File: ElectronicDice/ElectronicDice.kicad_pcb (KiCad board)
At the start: 2 copper layers, 17 parts, among them J1 Conn_01x02_Pin, SW1 SW_Push

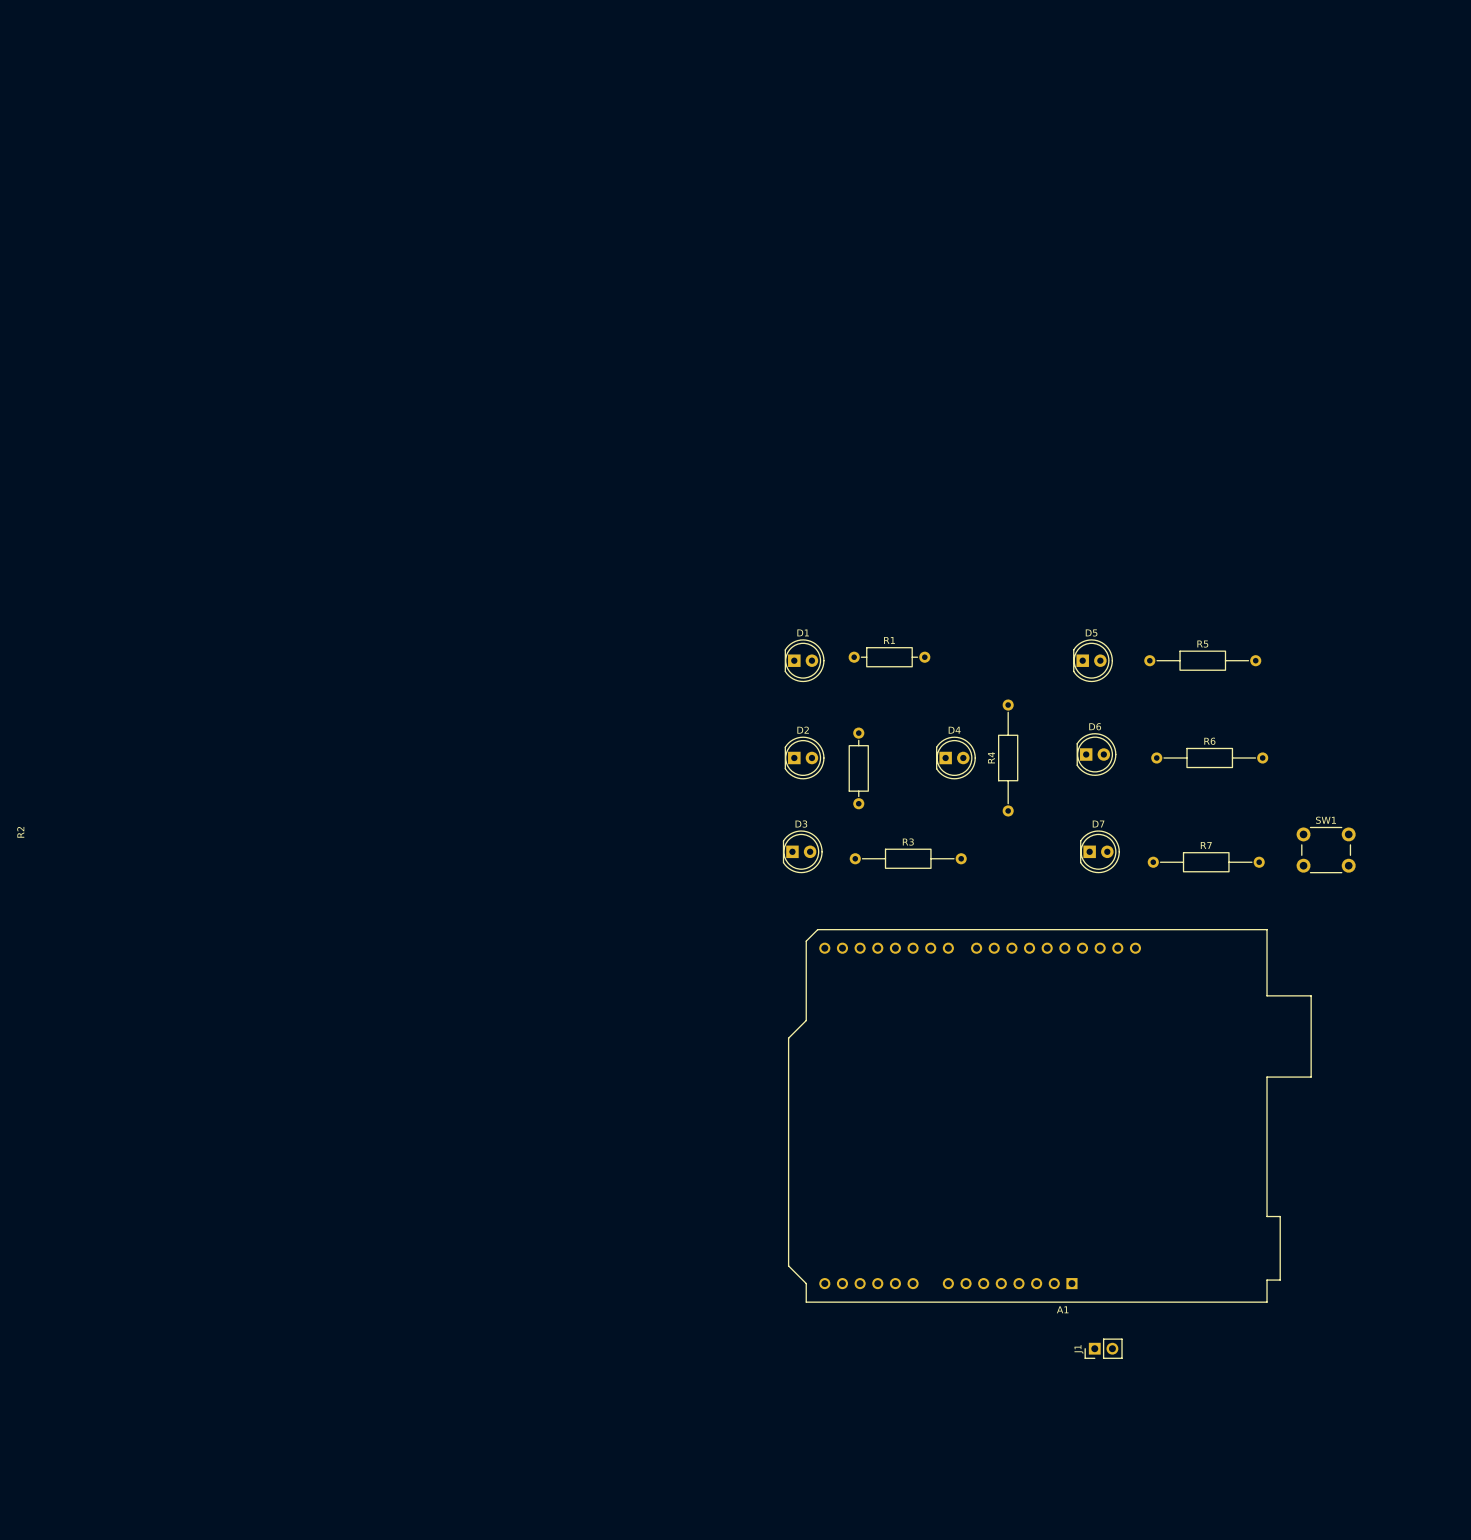
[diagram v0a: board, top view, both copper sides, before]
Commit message: Added connections in PCB
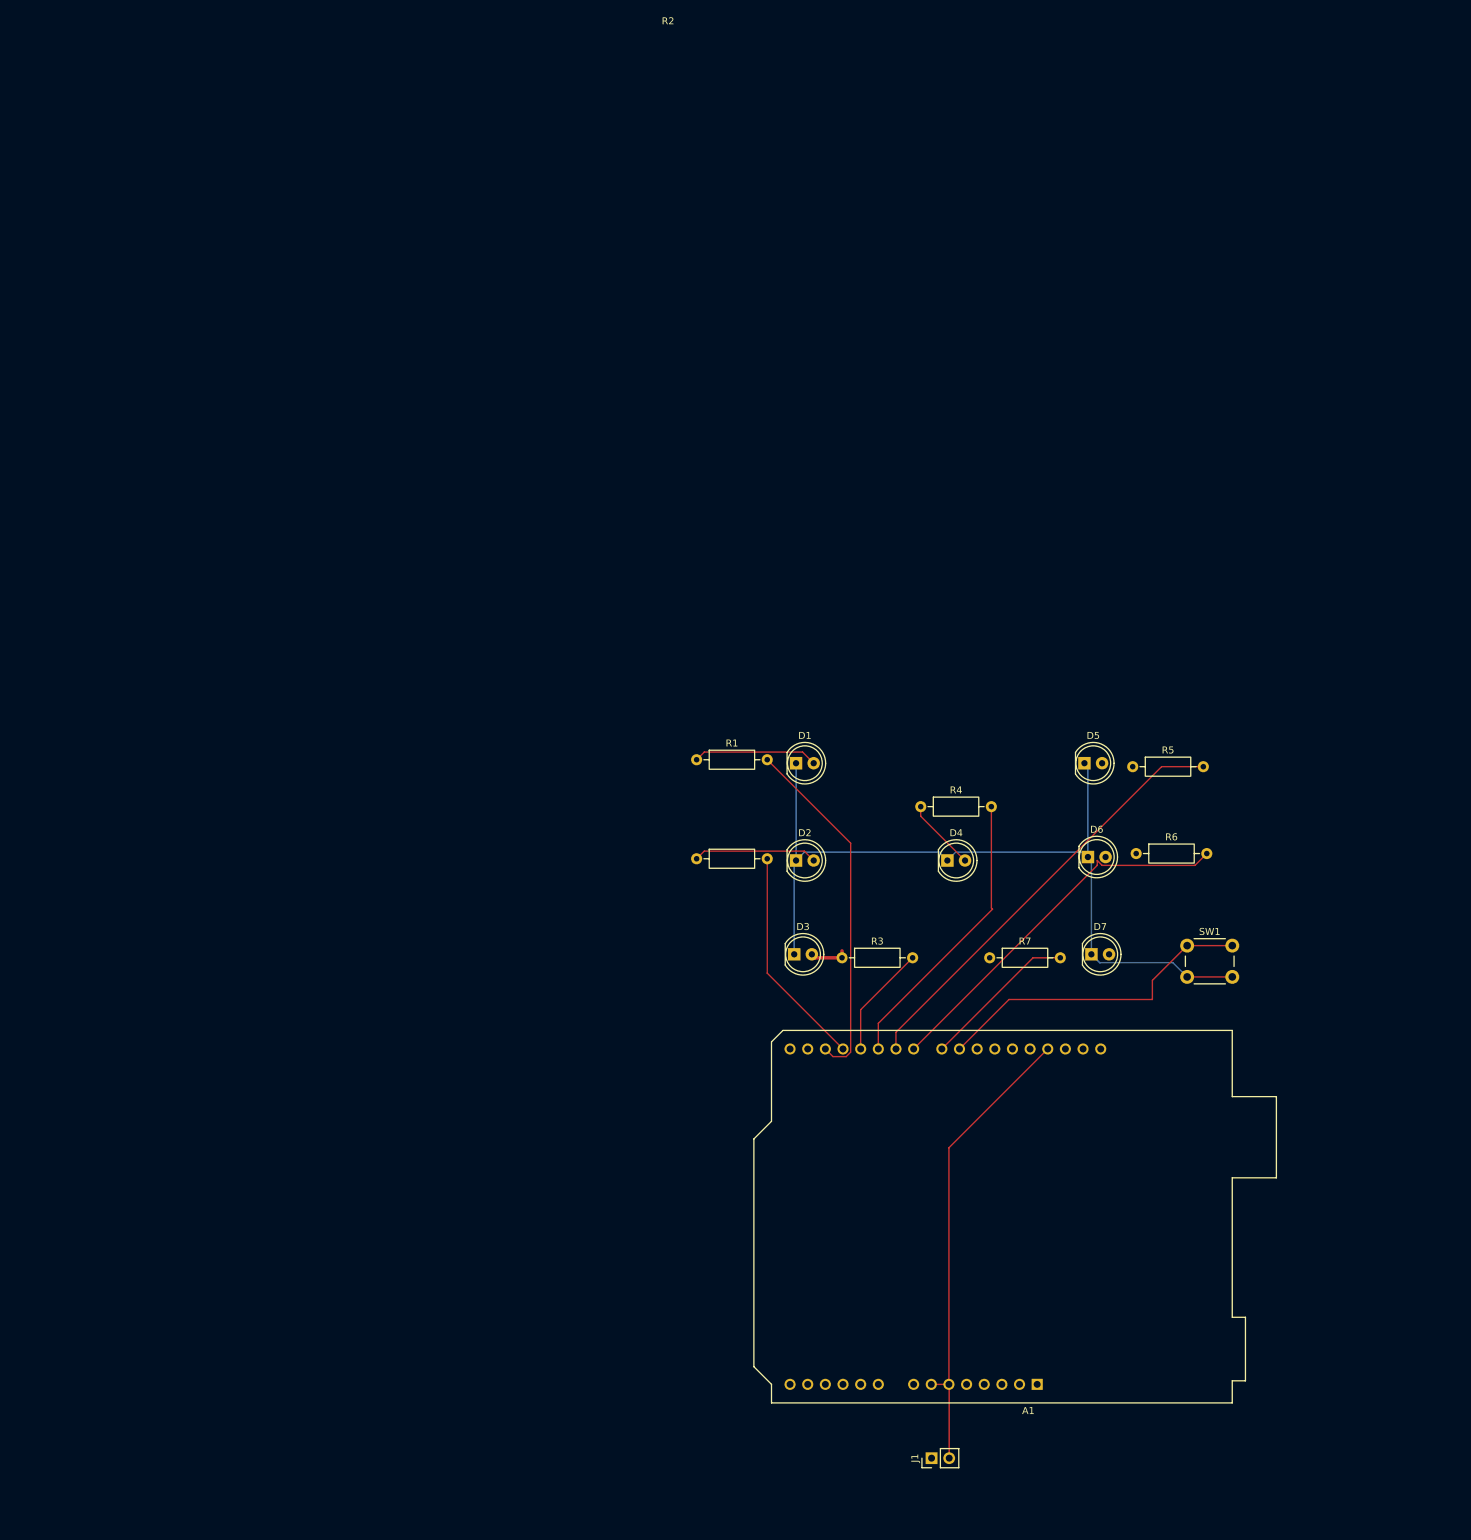
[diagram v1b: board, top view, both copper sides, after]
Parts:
- R3, R4, R5, R6, R7: footprint Resistor_THT:R_Axial_DIN0207_L6.3mm_D2.5mm_P15.24mm_Horizontal -> Resistor_THT:R_Axial_DIN0207_L6.3mm_D2.5mm_P10.16mm_Horizontal
- moved J1 28.3 mm to (109.5, 140.2)
- moved R7 27.3 mm to (117.8, 68.2)
- moved R1 27.0 mm to (75.7, 39.8)
- moved R2 24.6 mm to (75.7, 54.0), turned to 0 degrees
- moved SW1 23.2 mm to (146.2, 66.5)
- moved R5 15.4 mm to (138.4, 40.8)
- moved A1 15.3 mm to (124.7, 129.6)
- moved D1 14.8 mm to (90.0, 40.2)
- moved D2 14.8 mm to (90.0, 54.2)
- moved D3 14.8 mm to (89.7, 67.8)
- moved D4 14.8 mm to (111.8, 54.2)
- moved D5 14.8 mm to (131.5, 40.2)
- moved D6 14.8 mm to (132.0, 53.8)
- moved D7 14.8 mm to (132.5, 67.8)
- moved R3 14.4 mm to (96.6, 68.2)
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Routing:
- net GND: track 0.00 -> 188.3 mm
- net Net-(A1-D6): track 0.00 -> 62.5 mm
- net Net-(A1-D7): track 0.00 -> 54.8 mm
- net Net-(A1-D2): track 0.00 -> 51.4 mm
- net Net-(A1-D9): track 0.00 -> 47.0 mm
- net Net-(A1-D5): track 0.00 -> 41.7 mm
- net Net-(A1-D3): track 0.00 -> 31.9 mm
- net Net-(A1-D8): track 0.00 -> 22.5 mm
- net Net-(D1-A): track 0.00 -> 18.5 mm
- net Net-(D2-A): track 0.00 -> 17.9 mm
- net Net-(A1-D4): track 0.00 -> 16.2 mm
- net Net-(D4-A): track 0.00 -> 10.4 mm
- net Net-(D3-A): track 0.00 -> 5.55 mm
- net Net-(D6-A): track 0.00 -> 0.50 mm

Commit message: PCB design completed
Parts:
- added REF**: MountingHole_3.2mm_M3, MountingHole:MountingHole_3.2mm_M3, F.Cu at (63.0, 37.0)
- added REF**: MountingHole_3.2mm_M3, MountingHole:MountingHole_3.2mm_M3, F.Cu at (62.5, 139.5)
- added REF**: MountingHole_3.2mm_M3, MountingHole:MountingHole_3.2mm_M3, F.Cu at (169.5, 36.5)
- added REF**: MountingHole_3.2mm_M3, MountingHole:MountingHole_3.2mm_M3, F.Cu at (169.0, 140.5)
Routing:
- net Net-(D7-A): track 0.00 -> 46.4 mm
- net GND: track 188.3 -> 220.0 mm
- net +5V: track 0.00 -> 12.7 mm
- net Net-(D6-A): track 0.50 -> 5.11 mm
- net Net-(D5-A): track 0.00 -> 4.61 mm
- added copper zone on B.Cu, net GND
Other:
- board outline added: 143.5 x 124 mm

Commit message: added minor aesthetic changes to pcb
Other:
- board size 143.5 x 124 mm -> 119.5 x 115 mm
- board text added: "Electronic Dice - Devansh Verma (250331)"
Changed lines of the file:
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@@
 		(pcbplotparams
 			(layerselection 0x00000000_00000000_55555555_5755f5ff)
-			(plot_on_all_layers_selection 0x00000000_00000000_00000000_00000000)
+			(plot_on_all_layers_selection 0x00000000_00000000_00000000_0200a8ad)
 			(disableapertmacros no)
 			(usegerberextensions no)
@@
 			(crossoutdnponfab yes)
 			(subtractmaskfromsilk no)
-			(outputformat 1)
+			(outputformat 4)
 			(mirror no)
-			(drillshape 1)
+			(drillshape 0)
 			(scaleselection 1)
 			(outputdirectory "")
@@
 	)
 	(gr_line
-		(start 43 26)
-		(end 41.5 150)
+		(start 56 31)
+		(end 55.5 146)
 		(stroke
 			(width 0.05)
-			(type default)
+			(type solid)
 		)
 		(layer "Edge.Cuts")
 	)
 	(gr_line
-		(start 43 26)
-		(end 185 26.5)
+		(start 56 31)
+		(end 175 31)
 		(stroke
 			(width 0.05)
@@
 	)
 	(gr_line
-		(start 185 26.5)
-		(end 185 150)
+		(start 174.5 145.5)
+		(end 55.5 146)
 		(stroke
 			(width 0.05)
@@
 	)
 	(gr_line
-		(start 185 150)
-		(end 41.5 150)
+		(start 175 31)
+		(end 174.5 145.5)
 		(stroke
 			(width 0.05)
@@
 		(layer "Edge.Cuts")
 	)
+	(gr_text "Electronic Dice - Devansh Verma (250331)"
+		(at 93.5 34.5 0)
+		(layer "F.SilkS")
+		(effects
+			(font
+				(size 1.5 1.5)
+				(thickness 0.15)
+			)
+			(justify left bottom)
+		)
+	)
 	(segment
 		(start 91.165 52.9)
@@
 		)
 		(min_thickness 0.25)
-		(fill
+		(fill yes
 			(thermal_gap 0.5)
 			(thermal_bridge_width 0.5)
+			(smoothing fillet)
+			(radius 8)
 			(island_removal_mode 0)
 		)
 		(polygon
 			(pts
-				(xy 55.994764 31.010887) (xy 55.878658 145.379577) (xy 174.5 145.5) (xy 174.5 31)
+				(xy 56.105674 31.039776) (xy 55.810151 145.192732) (xy 174.606526 145.426572) (xy 174.831065 31.35556)
 			)
 		)
